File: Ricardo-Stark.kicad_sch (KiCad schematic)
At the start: 37 parts, among them J1 RBUS, U1 ESP32-S3, Y1 R940000171

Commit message: v1.2
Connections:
- net ADS_CLK: now also U1.37 (SPICLK_P/GPIO47); no longer U1.24 (GPIO18/ADC2_CH7/DAC_1)
- net ADS_CS0: now also U1.42 (GPIO37); no longer U1.27 (GPIO21)
- net BUCKC_EN: now also U1.17 (GPIO12/ADC2_CH1); no longer U1.18 (GPIO13/ADC2_CH2)
- net BUCKP_EN: no longer U1.19 (GPIO14/ADC2_CH3)
- net BuckPGOOD: now also U1.31 (SPIWP/GPIO28); no longer U1.37 (SPICLK_P/GPIO47)
- net HSPI_MOSI: now also U1.38 (GPIO33); no longer U1.40 (GPIO35)
- net HSPI_SCLK: now also U1.40 (GPIO35); no longer U1.38 (GPIO33)
- net SD1_CS: now also U1.35 (SPID/GPIO32); no longer U1.34 (SPIQ/GPIO31)
- net ServoV_LOG: now also U1.18 (GPIO13/ADC2_CH2); no longer U1.17 (GPIO12/ADC2_CH1)
- net VSPI_MISO: now also U1.32 (SPICS0/GPIO29); no longer U1.31 (SPIWP/GPIO28)
- net VSPI_MOSI: now also U1.34 (SPIQ/GPIO31); no longer U1.33 (SPICLK/GPIO30)
- net VSPI_SCLK: now also U1.33 (SPICLK/GPIO30); no longer U1.32 (SPICS0/GPIO29)
- new net BuckP_EN: U1.27 (GPIO21)
- no-connect marks 17 -> 16
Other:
- sheet buckC ports: added BUCKC_EN; removed BUCK_EN

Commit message: More Based
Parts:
- added ArcReactorCore1, Eye1, Eye2: Blue_LED, Resistor_SMD:R_0402_1005Metric, symbol Device:LED_Small
- added CANRXLED1: CANRXLED, LED_SMD:LED_0402_1005Metric, symbol Device:LED_Small
- added CANTXLED1: CANTXLED, LED_SMD:LED_0402_1005Metric, symbol Device:LED_Small
- added R11, R12, R13, R14: 3k, Resistor_SMD:R_0402_1005Metric, symbol Device:R_Small
- added R2, R3: 1k, Resistor_SMD:R_0402_1005Metric, symbol Device:R_Small
- added Repulsor1, Repulsor2: White_LED, Resistor_SMD:R_0402_1005Metric, symbol Device:LED_Small
- renumbered R8 to R10, R2 to R4, R3 to R5, R4 to R6, R5 to R7, R6 to R8, R7 to R9
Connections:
- net +3V3: now also R11.1, R12.1, R13.1, R14.1, R2.1, R3.1
- net CAN_RX: now also CANRXLED1.1 (K)
- net CAN_TX: now also CANTXLED1.1 (K)
- net GND: now also ArcReactorCore1.1 (K), Eye1.1 (K), Eye2.1 (K), Repulsor1.1 (K), Repulsor2.1 (K)
- net ServoBuckPGood: now reaches U1.19 (GPIO14/ADC2_CH3)
- net SD1_DET: now reaches U1.24 (GPIO18/ADC2_CH7/DAC_1)
- net BuckPGOOD renamed ServoBuckPGOOD
- net ServoBuckPGOOD: no longer U1.31 (SPIWP/GPIO28)
- new net: CANRXLED1.2 (A), R3.2
- new net: CANTXLED1.2 (A), R2.2
- new net: R13.2, Repulsor2.2 (A)
- new net: R12.2, Repulsor1.2 (A)
- new net: Eye1.2 (A), Eye2.2 (A), R14.2
- new net: ArcReactorCore1.2 (A), R11.2
- new net PyroBuckPGOOD: U1.31 (SPIWP/GPIO28)
- no-connect marks 16 -> 14
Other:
- sheet microSD ports: added SD1_DET; removed none
- moved on the sheet: TP1, TP2

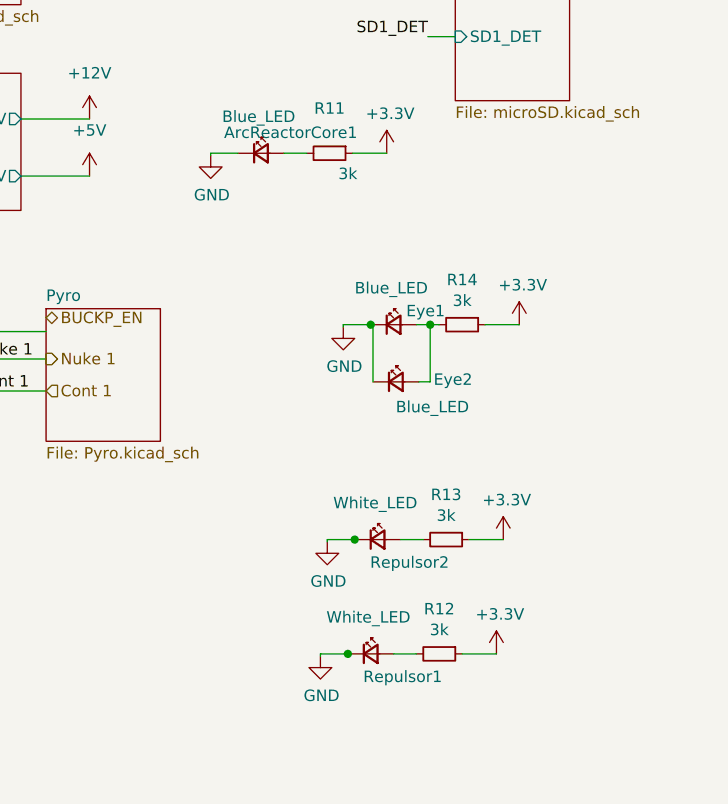
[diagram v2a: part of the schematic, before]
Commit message: changed led resistances
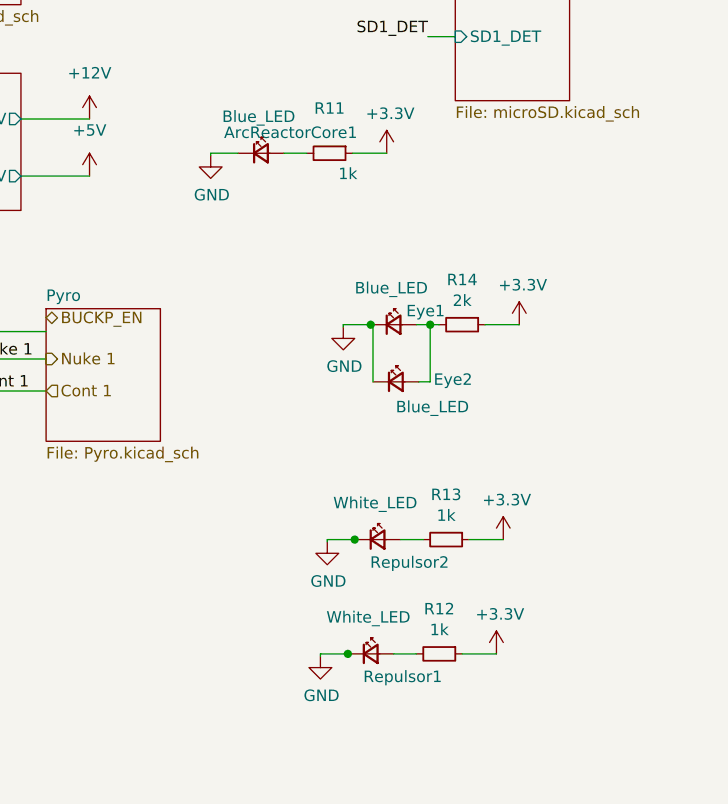
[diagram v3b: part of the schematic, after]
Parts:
- R11, R12, R13: value 3k -> 1k
- R14: value 3k -> 2k
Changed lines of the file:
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@@
       (effects (font (size 1.27 1.27)))
     )
-    (property "Value" "3k" (at 261.112 120.523 90)
+    (property "Value" "2k" (at 261.112 120.523 90)
       (effects (font (size 1.27 1.27)))
     )
@@
       (effects (font (size 1.27 1.27)))
     )
-    (property "Value" "3k" (at 258.572 157.099 90)
+    (property "Value" "1k" (at 258.572 157.099 90)
       (effects (font (size 1.27 1.27)))
     )
@@
       (effects (font (size 1.27 1.27)))
     )
-    (property "Value" "3k" (at 259.334 144.399 90)
+    (property "Value" "1k" (at 259.334 144.399 90)
       (effects (font (size 1.27 1.27)))
     )
@@
       (effects (font (size 1.27 1.27)))
     )
-    (property "Value" "3k" (at 248.412 106.426 90)
-      (effects (font (size 1.27 1.27)))
-    )
+    (property "Value" "1k" (at 248.412 106.426 90)
+      (effects (font (size 1.27 1.27)))
+    )

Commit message: Most Review 1 changes made
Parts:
- added R20: 54.9R, Resistor_SMD:R_0402_1005Metric, symbol Device:R_Small
- R14: value 2k -> 3k
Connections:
- net ADS_CLK: now also R20.1; no longer U1.37 (SPICLK_P/GPIO47)
- net BuckP_EN: now also U1.26 (GPIO20/USB_D+/ADC2_CH9); no longer U1.27 (GPIO21)
- net Cont 1: now also U1.28 (SPI_CS1/GPIO26); no longer U1.30 (SPIHD/GPIO27)
- net Data+: now also U1.25 (GPIO19/USB_D-/ADC2_CH8); no longer U1.26 (GPIO20/USB_D+/ADC2_CH9)
- net Data-: now also U1.24 (GPIO18/ADC2_CH7/DAC_1); no longer U1.25 (GPIO19/USB_D-/ADC2_CH8)
- net Nuke 1: now also U1.27 (GPIO21); no longer U1.28 (SPI_CS1/GPIO26)
- net SD1_CS: now also U1.48 (MTMS/JTAG/GPIO42); no longer U1.35 (SPID/GPIO32)
- net SD1_DET: now also U1.23 (GPIO17/ADC2_CH6/DAC_2); no longer U1.24 (GPIO18/ADC2_CH7/DAC_1)
- net VSPI_MISO: now also U1.21 (GPIO15/ADC2_CH4/XTAL_32K_P); no longer U1.32 (SPICS0/GPIO29)
- net VSPI_MOSI: now also U1.45 (MTDO/JTAG/GPIO40); no longer U1.34 (SPIQ/GPIO31)
- net VSPI_SCLK: now also U1.47 (MTDI/JTAG/GPIO41); no longer U1.33 (SPICLK/GPIO30)
- net PyroBuckPGOOD: no longer names the net of U1.31 (SPIWP/GPIO28)
- new net: R20.2, U1.37 (SPICLK_P/GPIO47)
- no-connect marks 14 -> 16

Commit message: Review 1 Changes Complete
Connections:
- net +12V: no longer J1.4 (Pin_4), R8.1
- new net DeployV: J1.4 (Pin_4), R8.1
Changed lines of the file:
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@@
   (no_connect (at 135.89 80.01))
   (no_connect (at 135.89 102.87))
-  (wire (pts (xy 120.65 25.4) (xy 120.65 35.56))
-    (stroke (width 0) (type default))
-  )
   (wire (pts (xy 30.48 191.77) (xy 30.48 190.5))
     (stroke (width 0) (type default))
@@
   (label "HSPI_MOSI" (at 135.89 95.25 0) (fields_autoplaced)
     (effects (font (size 1.27 1.27)) (justify left bottom))
+  )
+  (global_label "DeployV" (shape bidirectional) (at 73.66 26.67 0) (fields_autoplaced)
+    (effects (font (size 1.27 1.27)) (justify left))
+    (property "Intersheetrefs" "${INTERSHEET_REFS}" (at 84.3215 26.67 0)
+      (effects (font (size 1.27 1.27)) (justify left) hide)
+    )
+  )
+  (global_label "DeployV" (shape bidirectional) (at 120.65 25.4 270) (fields_autoplaced)
+    (effects (font (size 1.27 1.27)) (justify right))
+    (property "Intersheetrefs" "${INTERSHEET_REFS}" (at 120.65 36.0615 90)
+      (effects (font (size 1.27 1.27)) (justify right) hide)
+    )
   )
   (global_label "RBUS_uC_V" (shape input) (at 123.19 25.4 270) (fields_autoplaced)
@@
     )
   )
-  (symbol (lib_id "power:+12V") (at 73.66 26.67 0) (unit 1)
-    (in_bom yes) (on_board yes) (dnp no)
-    (property "Reference" "#PWR014" (at 73.66 30.48 0)
-      (effects (font (size 1.27 1.27)) hide)
-    )
-    (property "Value" "+12V" (at 73.66 21.59 0)
-      (effects (font (size 1.27 1.27)))
-    )
-    (property "Footprint" "" (at 73.66 26.67 0)
-      (effects (font (size 1.27 1.27)) hide)
-    )
-    (property "Datasheet" "" (at 73.66 26.67 0)
-      (effects (font (size 1.27 1.27)) hide)
-    )
-    (pin "1")
-    (instances
-      (project "Ricardo-Stark"
-        (path "/7db990e4-92e1-4f99-b4d2-435bbec1ba83"
-          (reference "#PWR014") (unit 1)
-        )
-      )
-    )
-  )
   (symbol (lib_id "Mechanical:MountingHole_Pad") (at 278.13 30.48 0) (unit 1)
     (in_bom yes) (on_board yes) (dnp no)
@@
         )
       )
-    )
-  )
-  (symbol (lib_id "power:+12V") (at 120.65 35.56 180) (unit 1)
-    (in_bom yes) (on_board yes) (dnp no)
-    (property "Reference" "#PWR015" (at 120.65 31.75 0)
-      (effects (font (size 1.27 1.27)) hide)
-    )
-    (property "Value" "+12V" (at 120.65 41.91 90)
-      (effects (font (size 1.27 1.27)))
-    )
-    (property "Footprint" "" (at 120.65 35.56 0)
-      (effects (font (size 1.27 1.27)) hide)
-    )
-    (property "Datasheet" "" (at 120.65 35.56 0)
-      (effects (font (size 1.27 1.27)) hide)
-    )
-    (pin "1")
-    (instances
-      (project "Ricardo-Stark"
-        (path "/7db990e4-92e1-4f99-b4d2-435bbec1ba83"
-          (reference "#PWR015") (unit 1)
-        )
-      )

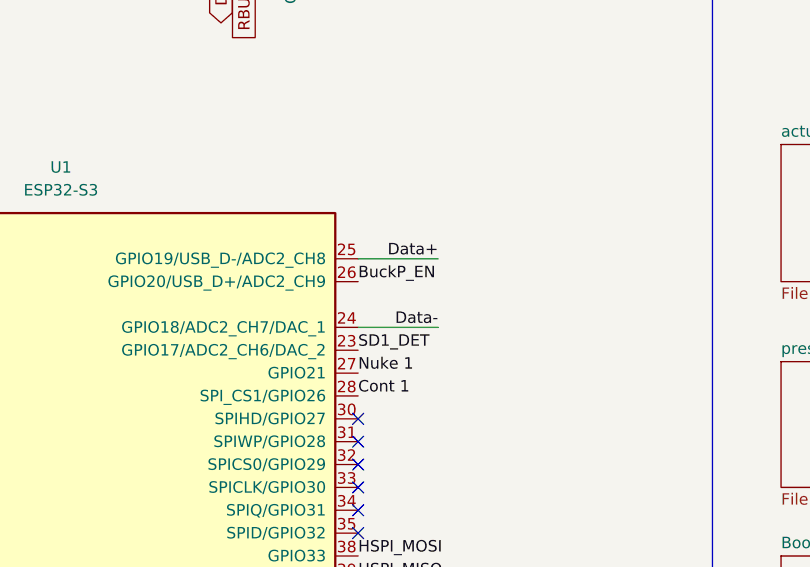
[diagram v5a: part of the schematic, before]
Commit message: Fixed USB tracks
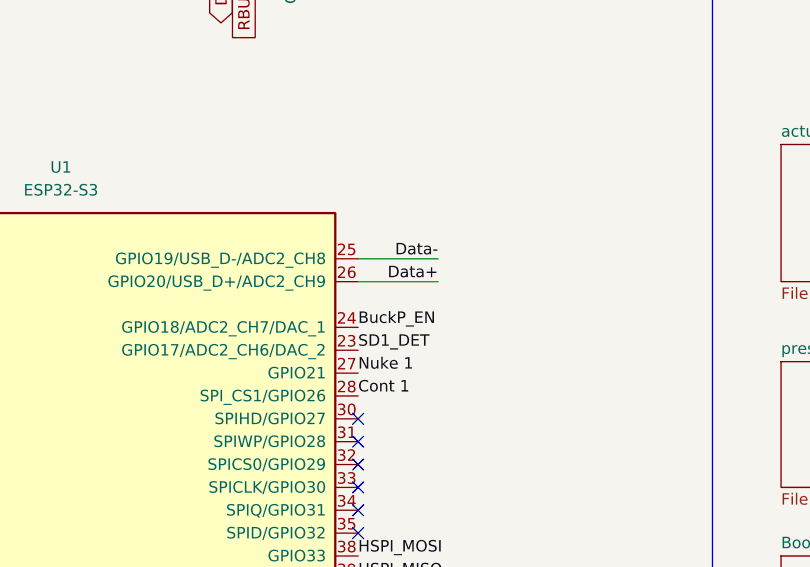
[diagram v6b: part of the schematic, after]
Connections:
- net BuckP_EN: now also U1.24 (GPIO18/ADC2_CH7/DAC_1); no longer U1.26 (GPIO20/USB_D+/ADC2_CH9)
- net Data+: now also U1.26 (GPIO20/USB_D+/ADC2_CH9); no longer U1.25 (GPIO19/USB_D-/ADC2_CH8)
- net Data-: now also U1.25 (GPIO19/USB_D-/ADC2_CH8); no longer U1.24 (GPIO18/ADC2_CH7/DAC_1)
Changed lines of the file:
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@@
     (stroke (width 0) (type default))
   )
-  (wire (pts (xy 135.89 69.85) (xy 144.78 69.85))
+  (wire (pts (xy 135.89 64.77) (xy 144.78 64.77))
     (stroke (width 0) (type default))
   )
@@
     (effects (font (size 1.27 1.27)) (justify left bottom))
   )
-  (label "BuckP_EN" (at 135.89 64.77 0) (fields_autoplaced)
+  (label "BuckP_EN" (at 135.89 69.85 0) (fields_autoplaced)
     (effects (font (size 1.27 1.27)) (justify left bottom))
   )
@@
     (effects (font (size 1.27 1.27)) (justify right bottom))
   )
-  (label "Data+" (at 144.78 62.23 180) (fields_autoplaced)
-    (effects (font (size 1.27 1.27)) (justify right bottom))
-  )
-  (label "Data-" (at 144.78 69.85 180) (fields_autoplaced)
-    (effects (font (size 1.27 1.27)) (justify right bottom))
-  )
+  (label "Data+" (at 144.78 64.77 180) (fields_autoplaced)
+    (effects (font (size 1.27 1.27)) (justify right bottom))
+  )
+  (label "Data-" (at 144.78 62.23 180) (fields_autoplaced)
+    (effects (font (size 1.27 1.27)) (justify right bottom))
+  )

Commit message: Take 3
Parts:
- removed R10: 2.2k, Resistor_SMD:R_0402_1005Metric, symbol Device:R_Small
- removed R9: 1.5k, Resistor_SMD:R_0402_1005Metric, symbol Device:R_Small
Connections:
- net ServoBuckPGood: no longer names the net of U1.19 (GPIO14/ADC2_CH3)
- no-connect marks 16 -> 17
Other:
- sheet Pyro ports: added BUCKP_EN, Cont1, Nuke 1; removed none
- sheet buckC ports: added none; removed PGOOD
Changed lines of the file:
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@@
   (no_connect (at 69.85 77.47))
   (no_connect (at 135.89 85.09))
+  (no_connect (at 69.85 105.41))
   (no_connect (at 135.89 87.63))
   (no_connect (at 69.85 62.23))
@@
     (stroke (width 0) (type default))
   )
-  (wire (pts (xy 214.884 122.428) (xy 207.264 122.428))
+  (wire (pts (xy 214.884 124.968) (xy 207.264 124.968))
     (stroke (width 0) (type default))
   )
@@
     (stroke (width 0) (type default))
   )
-  (wire (pts (xy 207.264 127) (xy 214.884 127))
+  (wire (pts (xy 207.264 132.588) (xy 214.884 132.588))
     (stroke (width 0) (type default))
   )
@@
     (stroke (width 0) (type default))
   )
-  (wire (pts (xy 218.44 30.48) (xy 218.44 34.29))
-    (stroke (width 0) (type default))
-  )
   (wire (pts (xy 278.13 33.02) (xy 273.05 33.02))
     (stroke (width 0) (type default))
@@
     (stroke (width 0) (type default))
   )
-  (wire (pts (xy 207.264 130.556) (xy 214.884 130.556))
+  (wire (pts (xy 207.264 128.778) (xy 214.884 128.778))
     (stroke (width 0) (type default))
   )
@@
   )
   (wire (pts (xy 212.09 100.33) (xy 219.71 100.33))
-    (stroke (width 0) (type default))
-  )
-  (wire (pts (xy 215.9 25.4) (xy 218.44 25.4))
     (stroke (width 0) (type default))
   )
@@
     (effects (font (size 1.27 1.27)) (justify right bottom))
   )
-  (label "Nuke 1" (at 207.264 127 0) (fields_autoplaced)
+  (label "Nuke 1" (at 207.264 132.588 0) (fields_autoplaced)
     (effects (font (size 1.27 1.27)) (justify left bottom))
   )
@@
     (effects (font (size 1.27 1.27)) (justify left bottom))
   )
-  (label "BUCKP_EN" (at 207.264 122.428 180) (fields_autoplaced)
+  (label "BUCKP_EN" (at 207.264 124.968 180) (fields_autoplaced)
     (effects (font (size 1.27 1.27)) (justify right bottom))
   )
@@
     (effects (font (size 1.27 1.27)) (justify left bottom))
   )
-  (label "Cont 1" (at 207.264 130.556 0) (fields_autoplaced)
+  (label "Cont 1" (at 207.264 128.778 0) (fields_autoplaced)
     (effects (font (size 1.27 1.27)) (justify left bottom))
   )
@@
     (effects (font (size 1.27 1.27)) (justify right bottom))
   )
-  (label "ServoBuckPGood" (at 69.85 105.41 180) (fields_autoplaced)
-    (effects (font (size 1.27 1.27)) (justify right bottom))
-  )
   (label "CAN_RX" (at 69.85 72.39 180) (fields_autoplaced)
     (effects (font (size 1.27 1.27)) (justify right bottom))
@@
   (label "GPIO4" (at 69.85 80.01 180) (fields_autoplaced)
     (effects (font (size 1.27 1.27)) (justify right bottom))
-  )
-  (label "ServoBuckPGOOD" (at 218.44 33.02 0) (fields_autoplaced)
-    (effects (font (size 1.27 1.27)) (justify left bottom))
   )
   (label "HSPI_MISO" (at 135.89 97.79 0) (fields_autoplaced)
@@
     )
   )
-  (hierarchical_label "BUCKP_EN" (shape bidirectional) (at 214.884 122.428 0) (fields_autoplaced)
-    (effects (font (size 1.27 1.27)) (justify left))
-  )
-  (hierarchical_label "Cont 1" (shape input) (at 214.884 130.556 0) (fields_autoplaced)
-    (effects (font (size 1.27 1.27)) (justify left))
-  )
-  (hierarchical_label "Nuke 1" (shape output) (at 214.884 127 0) (fields_autoplaced)
-    (effects (font (size 1.27 1.27)) (justify left))
-  )
   (symbol (lib_id "power:+3.3V") (at 30.48 182.88 0) (unit 1)
     (in_bom yes) (on_board yes) (dnp no)
@@
     )
   )
-  (symbol (lib_id "power:GND") (at 218.44 39.37 0) (unit 1)
-    (in_bom yes) (on_board yes) (dnp no)
-    (property "Reference" "#PWR021" (at 218.44 45.72 0)
-      (effects (font (size 1.27 1.27)) hide)
-    )
-    (property "Value" "GND" (at 218.567 43.7642 0)
-      (effects (font (size 1.27 1.27)))
-    )
-    (property "Footprint" "" (at 218.44 39.37 0)
-      (effects (font (size 1.27 1.27)) hide)
-    )
-    (property "Datasheet" "" (at 218.44 39.37 0)
-      (effects (font (size 1.27 1.27)) hide)
-    )
-    (pin "1")
-    (instances
-      (project "Ricardo-Stark"
-        (path "/7db990e4-92e1-4f99-b4d2-435bbec1ba83"
-          (reference "#PWR021") (unit 1)
-        )
-      )
-    )
-  )
   (symbol (lib_id "power:GND") (at 233.172 104.394 0) (unit 1)
     (in_bom yes) (on_board yes) (dnp no)
@@
         (path "/7db990e4-92e1-4f99-b4d2-435bbec1ba83"
           (reference "#PWR010") (unit 1)
-        )
-      )
-    )
-  )
-  (symbol (lib_id "Device:R_Small") (at 218.44 27.94 180) (unit 1)
-    (in_bom yes) (on_board yes) (dnp no)
-    (property "Reference" "R9" (at 223.4184 27.94 90)
-      (effects (font (size 1.27 1.27)))
-    )
-    (property "Value" "1.5k" (at 221.107 27.94 90)
-      (effects (font (size 1.27 1.27)))
-    )
-    (property "Footprint" "Resistor_SMD:R_0402_1005Metric" (at 218.44 27.94 0)
-      (effects (font (size 1.27 1.27)) hide)
-    )
-    (property "Datasheet" "~" (at 218.44 27.94 0)
-      (effects (font (size 1.27 1.27)) hide)
-    )
-    (pin "1")
-    (pin "2")
-    (instances
-      (project "Ricardo-Stark"
-        (path "/7db990e4-92e1-4f99-b4d2-435bbec1ba83"
-          (reference "R9") (unit 1)
         )
       )
@@
     )
   )
-  (symbol (lib_id "Device:R_Small") (at 218.44 36.83 180) (unit 1)
-    (in_bom yes) (on_board yes) (dnp no)
-    (property "Reference" "R10" (at 223.4184 36.83 90)
-      (effects (font (size 1.27 1.27)))
-    )
-    (property "Value" "2.2k" (at 221.107 36.83 90)
-      (effects (font (size 1.27 1.27)))
-    )
-    (property "Footprint" "Resistor_SMD:R_0402_1005Metric" (at 218.44 36.83 0)
-      (effects (font (size 1.27 1.27)) hide)
-    )
-    (property "Datasheet" "~" (at 218.44 36.83 0)
-      (effects (font (size 1.27 1.27)) hide)
-    )
-    (pin "1")
-    (pin "2")
-    (instances
-      (project "Ricardo-Stark"
-        (path "/7db990e4-92e1-4f99-b4d2-435bbec1ba83"
-          (reference "R10") (unit 1)
-        )
-      )
-    )
-  )
   (symbol (lib_id "power:+3.3V") (at 252.73 104.14 0) (unit 1)
     (in_bom yes) (on_board yes) (dnp no)
@@
       (effects (font (size 1.27 1.27)) (justify left top))
     )
+    (pin "BUCKP_EN" bidirectional (at 214.884 124.968 180)
+      (effects (font (size 1.27 1.27)) (justify left))
+    )
+    (pin "Cont1" output (at 214.884 128.778 180)
+      (effects (font (size 1.27 1.27)) (justify left))
+    )
+    (pin "Nuke 1" input (at 214.884 132.588 180)
+      (effects (font (size 1.27 1.27)) (justify left))
+    )
     (instances
       (project "Ricardo-Stark"
@@
       (effects (font (size 1.27 1.27)) (justify left top))
     )
-    (pin "PGOOD" output (at 215.9 25.4 0)
-      (effects (font (size 1.27 1.27)) (justify right))
-    )
     (pin "BUCKC_EN" input (at 215.9 21.59 0)
